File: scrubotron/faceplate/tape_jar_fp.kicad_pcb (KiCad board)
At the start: 2 copper layers, 68 x 68 mm, 4 parts

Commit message: Minor updates
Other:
- board text added: "JLCJLCJLCJLC"

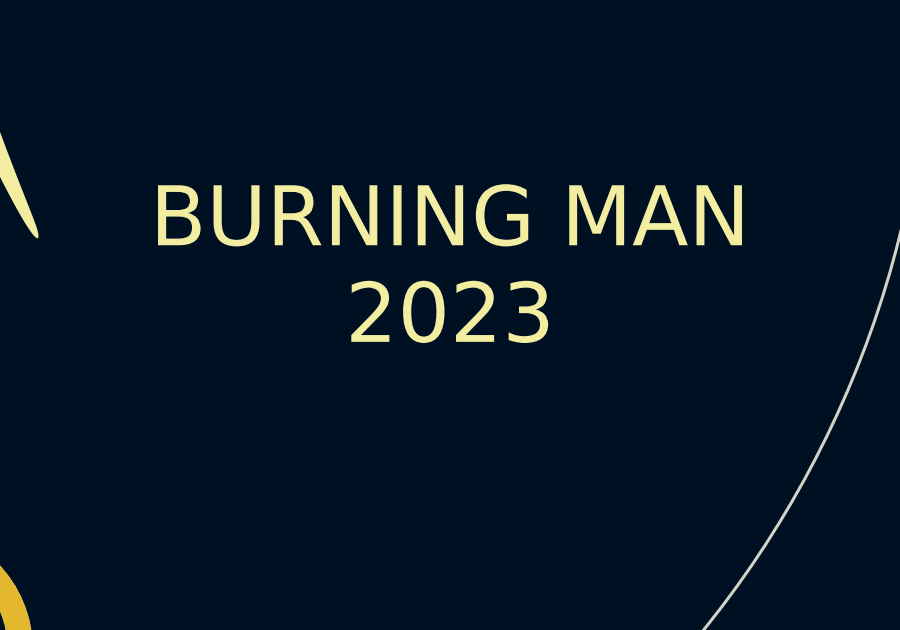
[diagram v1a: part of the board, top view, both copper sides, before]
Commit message: Fixed year on scrubotron
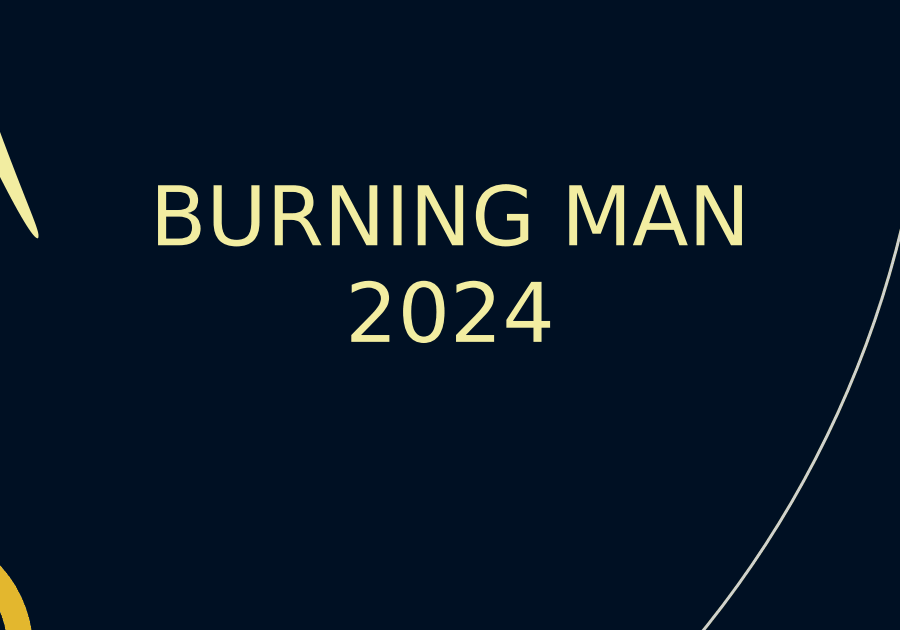
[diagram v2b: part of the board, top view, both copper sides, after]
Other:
- board text added: "BURNING MAN 2024"
- board text removed: "BURNING MAN 2023"
